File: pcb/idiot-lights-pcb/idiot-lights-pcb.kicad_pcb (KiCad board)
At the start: 2 copper layers, 100.3 x 66 mm, 82 parts, among them Q1 BSS138, Q10 BSS138, Q11 BSS138, Q12 BSS138, Q13 BSS138, Q14 BSS138, Q15 BSS138, Q16 BSS138, Q2 BSS138, Q3 BSS138, Q4 BSS138, Q5 BSS138, Q6 BSS138, Q7 BSS138, Q8 BSS138, Q9 BSS138, SW1 Toggle left indicator, SW2 Toggle right indicator, SW3 Toggle hazard warning, SW4 Break control, SW5 Reset, U1 RaspberryPi_Pico

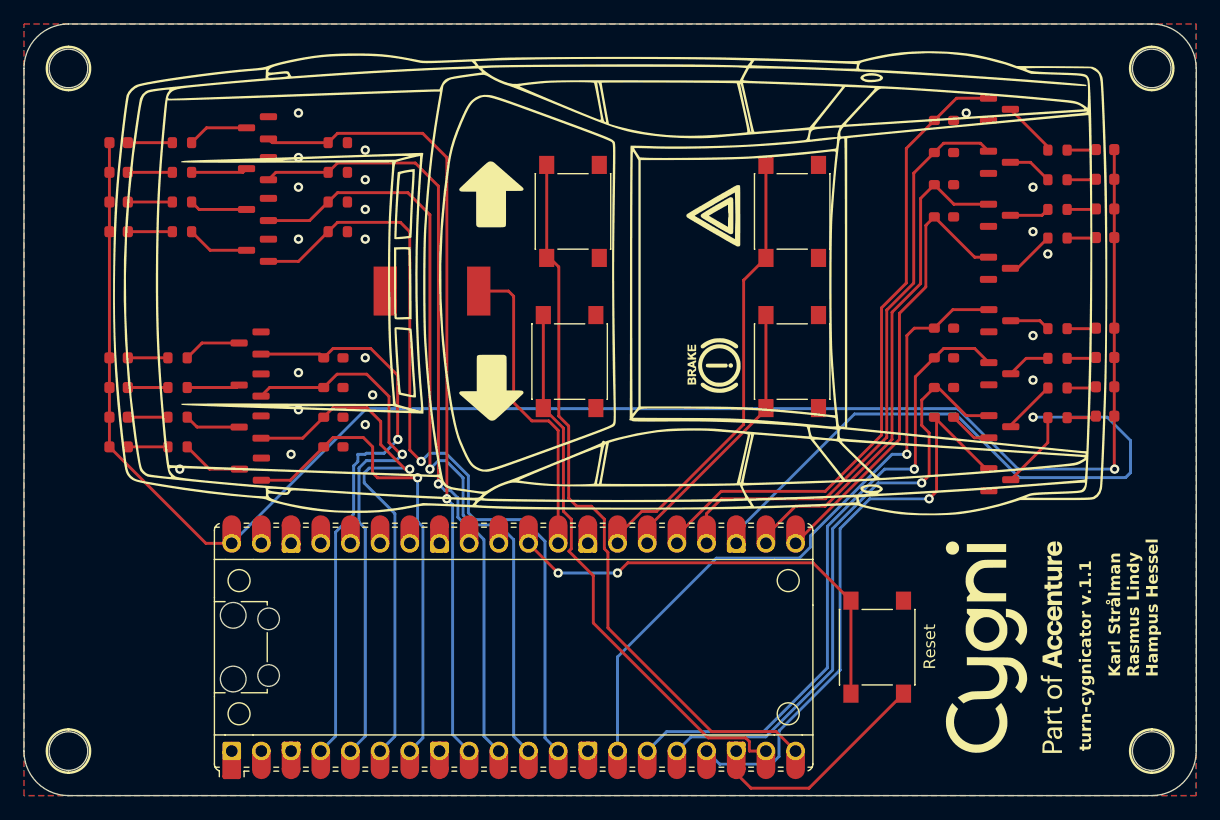
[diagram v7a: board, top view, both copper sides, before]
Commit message: Add gate resistors and re-reoute symbols
Bump version text to v.1.2
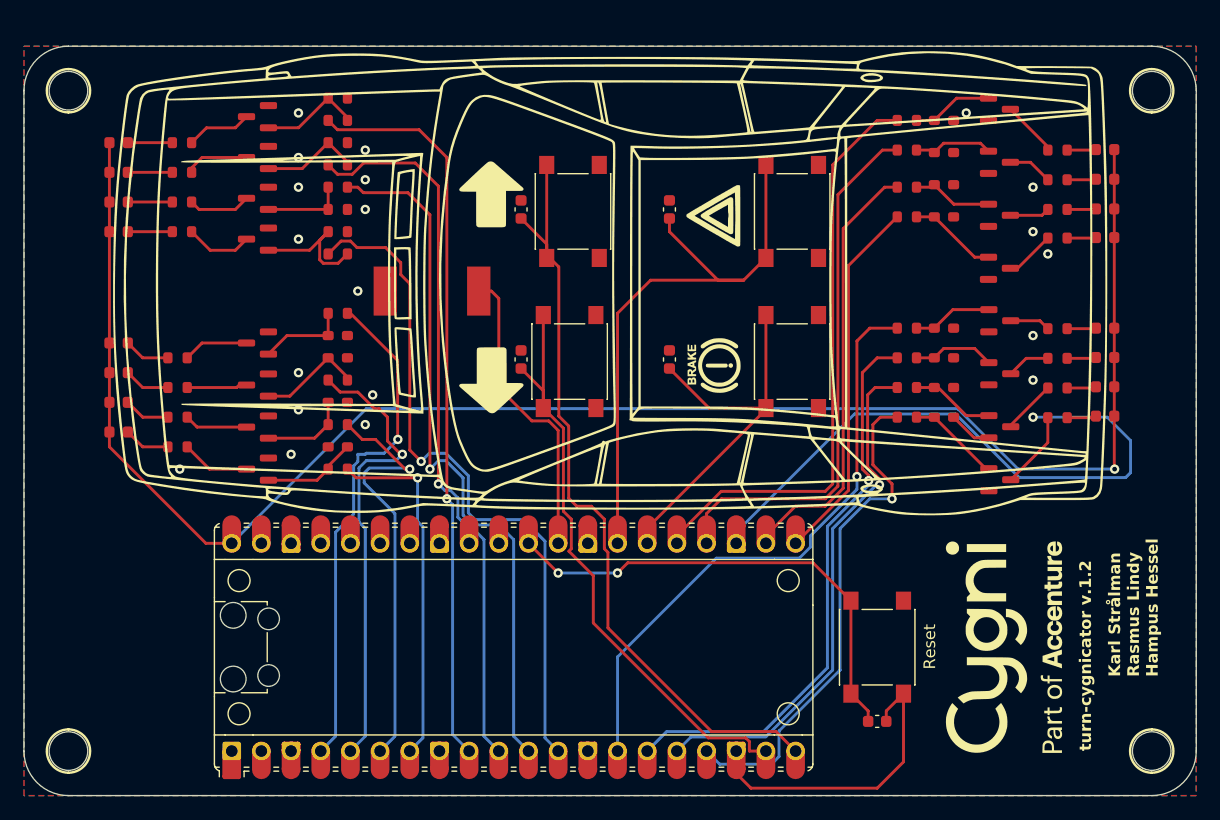
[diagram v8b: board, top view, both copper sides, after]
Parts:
- added C1: 100nF, Capacitor_SMD:C_0603_1608Metric, F.Cu at (177.2, 65.5)
- added C2: 100nF, Capacitor_SMD:C_0603_1608Metric, F.Cu at (177.2, 52.7)
- added C3: 100nF, Capacitor_SMD:C_0603_1608Metric, F.Cu at (189.9, 65.5)
- added C4: 100nF, Capacitor_SMD:C_0603_1608Metric, F.Cu at (189.9, 52.7)
- added C5: 100nF, Capacitor_SMD:C_0603_1608Metric, F.Cu at (207.6, 96.5)
- added R33: 3k3, Resistor_SMD_no_silk:R_0603_1608Metric_no_silk, F.Cu at (161.5, 61.6)
- added R34: 3k3, Resistor_SMD_no_silk:R_0603_1608Metric_no_silk, F.Cu at (161.5, 67.3)
- added R35: 3k3, Resistor_SMD_no_silk:R_0603_1608Metric_no_silk, F.Cu at (161.5, 71.1)
- added R36: 3k3, Resistor_SMD_no_silk:R_0603_1608Metric_no_silk, F.Cu at (161.5, 74.9)
- added R37: 3k3, Resistor_SMD_no_silk:R_0603_1608Metric_no_silk, F.Cu at (161.5, 45.1)
- added R38: 3k3, Resistor_SMD_no_silk:R_0603_1608Metric_no_silk, F.Cu at (161.5, 48.9)
- added R39: 3k3, Resistor_SMD_no_silk:R_0603_1608Metric_no_silk, F.Cu at (161.5, 50.8)
- added R40: 3k3, Resistor_SMD_no_silk:R_0603_1608Metric_no_silk, F.Cu at (161.5, 56.5)
- added R41: 3k3, Resistor_SMD_no_silk:R_0603_1608Metric_no_silk, F.Cu at (210.2, 62.9)
- added R42: 3k3, Resistor_SMD_no_silk:R_0603_1608Metric_no_silk, F.Cu at (210.2, 65.4)
- added R43: 3k3, Resistor_SMD_no_silk:R_0603_1608Metric_no_silk, F.Cu at (210.2, 67.9)
- added R44: 3k3, Resistor_SMD_no_silk:R_0603_1608Metric_no_silk, F.Cu at (210.2, 70.5)
- added R45: 3k3, Resistor_SMD_no_silk:R_0603_1608Metric_no_silk, F.Cu at (210.2, 45.1)
- added R46: 3k3, Resistor_SMD_no_silk:R_0603_1608Metric_no_silk, F.Cu at (210.2, 47.6)
- added R47: 3k3, Resistor_SMD_no_silk:R_0603_1608Metric_no_silk, F.Cu at (210.2, 50.8)
- added R48: 3k3, Resistor_SMD_no_silk:R_0603_1608Metric_no_silk, F.Cu at (210.2, 53.3)
- moved R9 3.81 mm to (161.5, 43.2)
- moved R3 2.57 mm to (161.5, 65.4)
- moved R11 2.54 mm to (161.5, 47.0)
- moved R1 1.94 mm to (161.5, 63.5)
- moved >NAME 1.91 mm to (231.1, 42.5)
- moved >NAME 1.91 mm to (138.4, 42.5)
- moved R5 1.33 mm to (161.5, 69.2)
- moved D4 1.27 mm to (142.7, 71.8)
- moved D1 1.27 mm to (142.7, 64.1)
- moved D2 1.27 mm to (142.7, 66.7)
- moved D3 1.27 mm to (142.7, 69.2)
- moved Q8 0.96 mm to (154.6, 55.2)
- moved Q5 0.95 mm to (154.6, 44.8)
- moved Q6 0.95 mm to (154.6, 48.3)
- moved Q7 0.95 mm to (154.6, 51.8)
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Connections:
- Q1 pad 1: /FL0 -> Net-(Q1-G)
- Q10 pad 1: /RL1 -> Net-(Q10-G)
- Q11 pad 1: /RL2 -> Net-(Q11-G)
- Q12 pad 1: /RL3 -> Net-(Q12-G)
- Q13 pad 1: /RR0 -> Net-(Q13-G)
- Q14 pad 1: /RR1 -> Net-(Q14-G)
- Q15 pad 1: /RR2 -> Net-(Q15-G)
- Q16 pad 1: /RR3 -> Net-(Q16-G)
- Q2 pad 1: /FL1 -> Net-(Q2-G)
- Q3 pad 1: /FL2 -> Net-(Q3-G)
- Q4 pad 1: /FL3 -> Net-(Q4-G)
- Q5 pad 1: /FR0 -> Net-(Q5-G)
- Q6 pad 1: /FR1 -> Net-(Q6-G)
- Q7 pad 1: /FR2 -> Net-(Q7-G)
- Q8 pad 1: /FR3 -> Net-(Q8-G)
- Q9 pad 1: /RL0 -> Net-(Q9-G)
- R1 pad 1: /FL0 -> Net-(Q1-G)
- R11 pad 1: /FR1 -> Net-(Q6-G)
- R13 pad 1: /FR2 -> Net-(Q7-G)
- R15 pad 1: /FR3 -> Net-(Q8-G)
- R17 pad 1: /RL0 -> Net-(Q9-G)
- R19 pad 1: /RL1 -> Net-(Q10-G)
- R21 pad 1: /RL2 -> Net-(Q11-G)
- R23 pad 1: /RL3 -> Net-(Q12-G)
- R25 pad 1: /RR0 -> Net-(Q13-G)
- R27 pad 1: /RR1 -> Net-(Q14-G)
- R29 pad 1: /RR2 -> Net-(Q15-G)
- R3 pad 1: /FL1 -> Net-(Q2-G)
- R31 pad 1: /RR3 -> Net-(Q16-G)
- R5 pad 1: /FL2 -> Net-(Q3-G)
- R7 pad 1: /FL3 -> Net-(Q4-G)
- R9 pad 1: /FR0 -> Net-(Q5-G)
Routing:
- net /HAZARD_BTN: track 37.7 -> 50.7 mm
- net /FL3: track 41.7 -> 30.4 mm
- net Net-(Q8-G): track 0.00 -> 11.3 mm
- net /FL2: track 46.7 -> 36.4 mm
- net /BREAK_BTN: track 22.3 -> 32.0 mm
- net Net-(Q2-G): track 0.00 -> 8.80 mm
- net /FR3: track 68.2 -> 59.5 mm
- net Net-(Q5-G): track 0.00 -> 8.49 mm
- net Net-(Q6-G): track 0.00 -> 8.36 mm
- net Net-(Q12-G): track 0.00 -> 8.01 mm
- net /FL1: track 47.2 -> 39.4 mm
- net Net-(Q4-G): track 0.00 -> 7.84 mm
- net Net-(Q1-G): track 0.00 -> 7.67 mm
- net /RL2: track 52.4 -> 44.8 mm
- net Net-(Q16-G): track 0.00 -> 7.59 mm
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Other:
- board size 100.3 x 66 mm -> 100.3 x 64.1 mm
- board text added: "turn-cygnicator v.1.2"
- board text removed: "turn-cygnicator v.1.1"
